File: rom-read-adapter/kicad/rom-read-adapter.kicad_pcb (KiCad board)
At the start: 2 copper layers, 100 x 100 mm, 27 parts

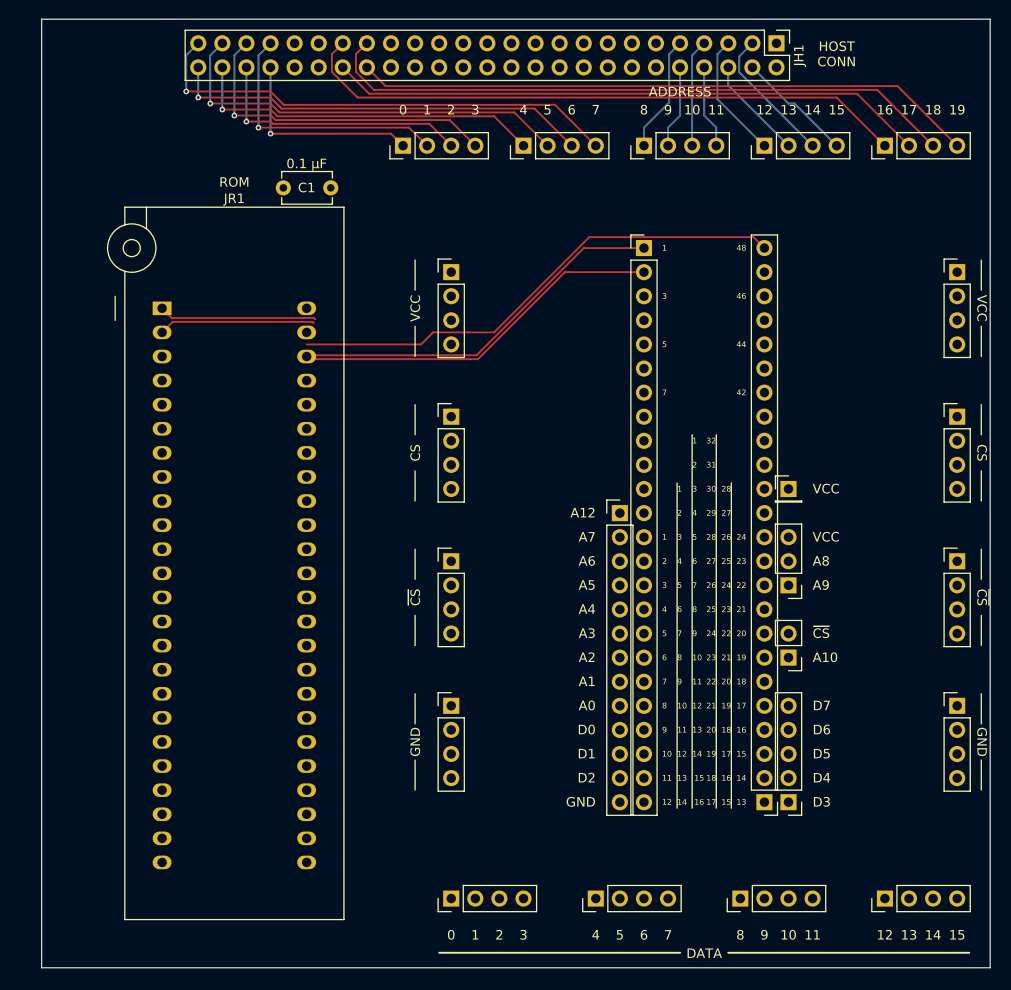
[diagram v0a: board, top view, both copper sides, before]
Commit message: WIP rom-read-adapter pcb: Add VCC/GND netclass; route D0-D8 non-default jumpers
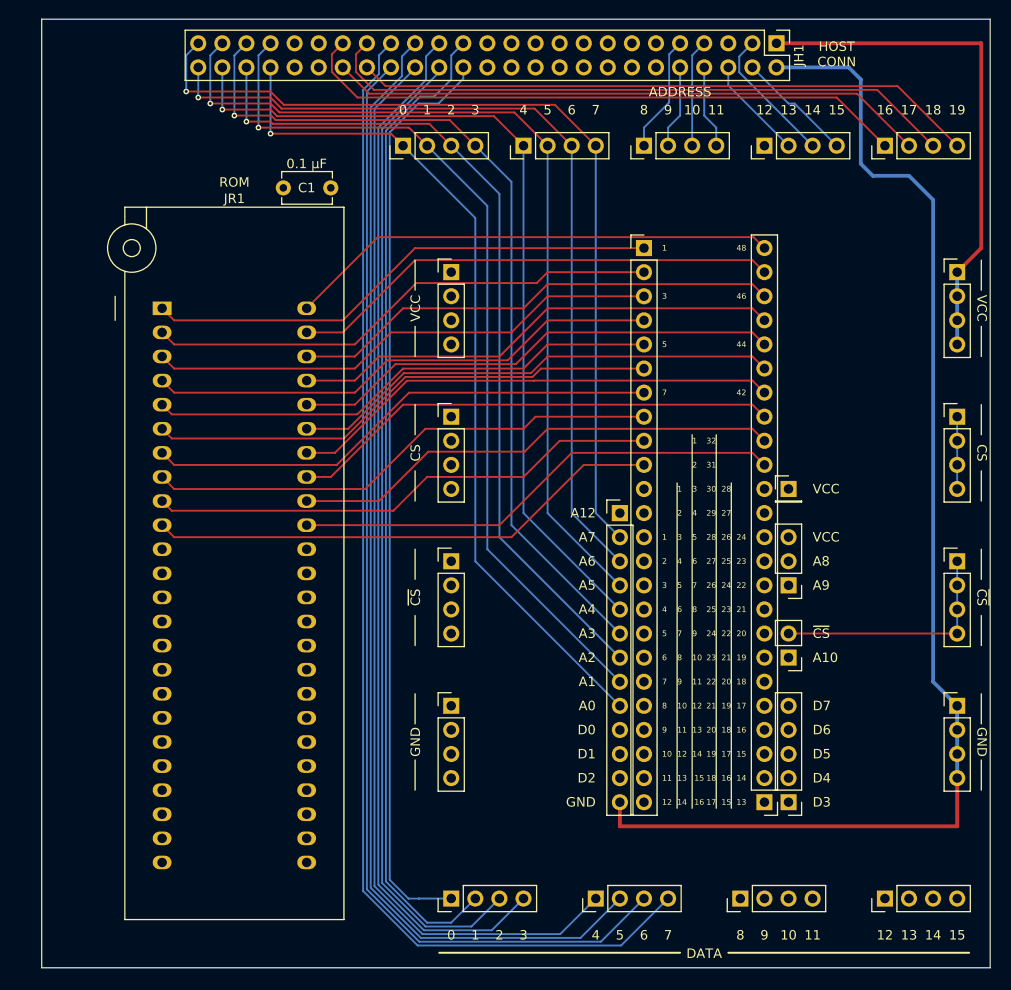
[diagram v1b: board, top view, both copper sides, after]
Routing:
- net GND: track 0.00 -> 132.7 mm
- net D7: track 0.00 -> 127.2 mm
- net D5: track 0.00 -> 121.1 mm
- net D6: track 0.00 -> 121.1 mm
- net D4: track 0.00 -> 115.1 mm
- net D3: track 0.00 -> 110.0 mm
- net D1: track 0.00 -> 104.9 mm
- net D2: track 0.00 -> 104.0 mm
- net D0: track 0.01 -> 97.4 mm
- net A0: track 21.5 -> 90.0 mm
- net A1: track 28.0 -> 92.9 mm
- net A2: track 28.4 -> 89.7 mm
- net A3: track 34.9 -> 92.6 mm
- net Net-(JR1-Pin_8): track 0.00 -> 54.5 mm
- net Net-(JR1-Pin_7): track 0.00 -> 54.5 mm
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
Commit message: WIP rom-read-adapter pcb: More routing; hit default pins problem
The default pins are in the way of getting ZIF socket pads connected
ZIF work area pin pads. We may try doing only right side pins on top
layer from this point on, and routing through the bottom layer for the
left side pins.
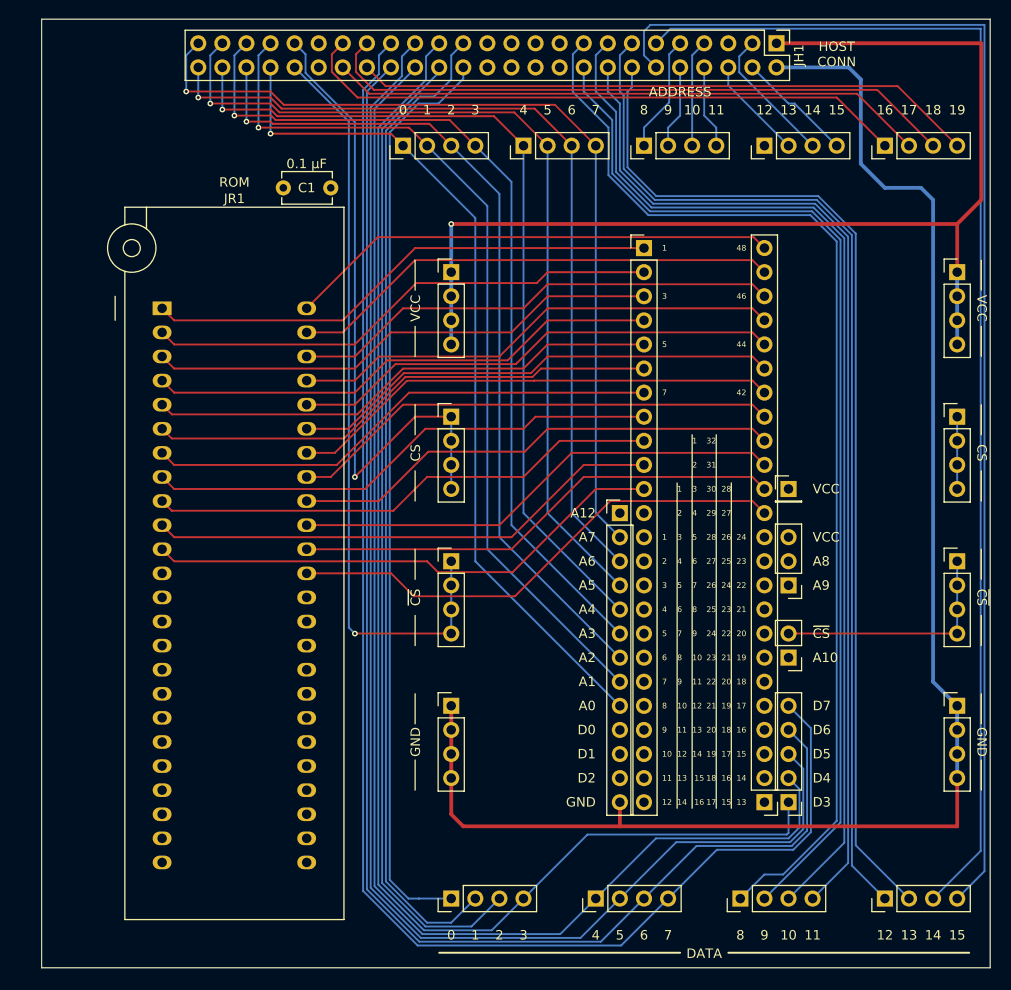
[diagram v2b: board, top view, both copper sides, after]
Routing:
- net D15: track 0.00 -> 133.8 mm
- net D14: track 0.00 -> 128.6 mm
- net D8: track 0.00 -> 117.5 mm
- net D10: track 0.00 -> 114.0 mm
- net D12: track 0.00 -> 112.3 mm
- net D9: track 0.00 -> 112.2 mm
- net D13: track 0.00 -> 110.1 mm
- net D11: track 0.00 -> 109.7 mm
- net ~{CS}: track 25.4 -> 105.5 mm, vias 0 -> 1
- net CS: track 7.62 -> 76.4 mm, vias 0 -> 1
- net VCC: track 54.4 -> 120.4 mm, vias 0 -> 1
- net Net-(JR1-Pin_11): track 0.00 -> 55.4 mm
- net Net-(JR1-Pin_37): track 0.00 -> 53.9 mm
- net Net-(JR1-Pin_38): track 0.00 -> 51.9 mm
- net D3: track 110.0 -> 144.1 mm
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
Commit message: WIP rom-read-adapter pcb: Routed ZIF 25-37 to work area, need to figure 12-24.
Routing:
- net Net-(JR1-Pin_35): track 0.00 -> 54.4 mm
- net Net-(JR1-Pin_36): track 0.00 -> 53.9 mm
- net Net-(JR1-Pin_34): track 0.00 -> 52.7 mm
- net Net-(JR1-Pin_28): track 0.00 -> 51.9 mm
- net Net-(JR1-Pin_26): track 0.00 -> 51.9 mm
- net Net-(JR1-Pin_32): track 0.00 -> 51.9 mm
- net Net-(JR1-Pin_31): track 0.00 -> 51.9 mm
- net Net-(JR1-Pin_30): track 0.00 -> 51.9 mm
- net Net-(JR1-Pin_27): track 0.00 -> 51.9 mm
- net Net-(JR1-Pin_33): track 0.00 -> 51.9 mm
- net Net-(JR1-Pin_29): track 0.00 -> 51.9 mm
- net Net-(JR1-Pin_25): track 0.00 -> 51.9 mm
- net D0: track 97.4 -> 122.6 mm
- net D1: track 104.9 -> 127.2 mm
- net D2: track 104.0 -> 123.4 mm
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
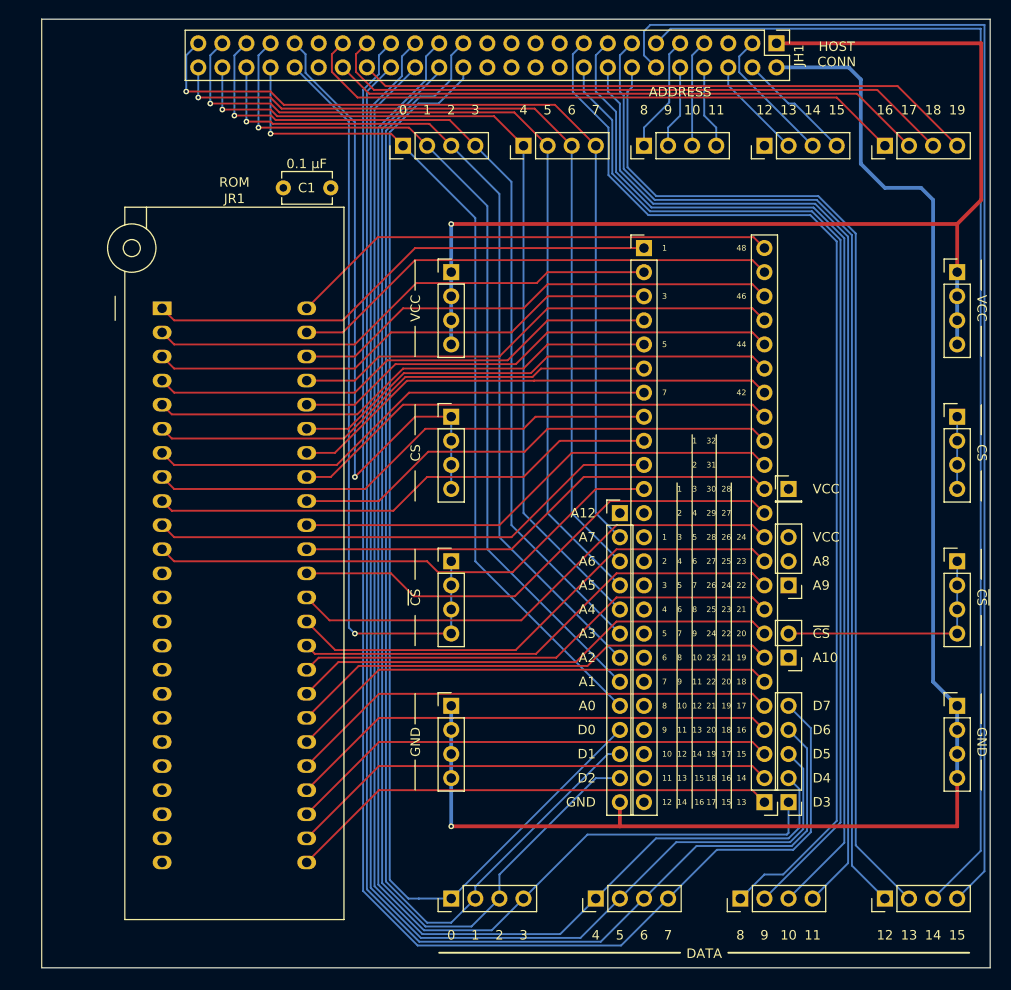
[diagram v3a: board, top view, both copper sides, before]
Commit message: WIP rom-read-adapter pcb: Everything routed except bypass cap
We need to figure out the best physical position for the bypass cap.
Ideally it should be as close as possible to the device pins
themselves, but we don't know which device pins are power; those are
determined half way across the board in the work area. So maybe place
it across the pin 12/24 GND and pin 24/24 VCC? Probably wants to be an
axial in that case, perhaps positioned top-to-bottom in the RHS
between the default jumpers and the VCC/CS/¬CS/GND jumpers.
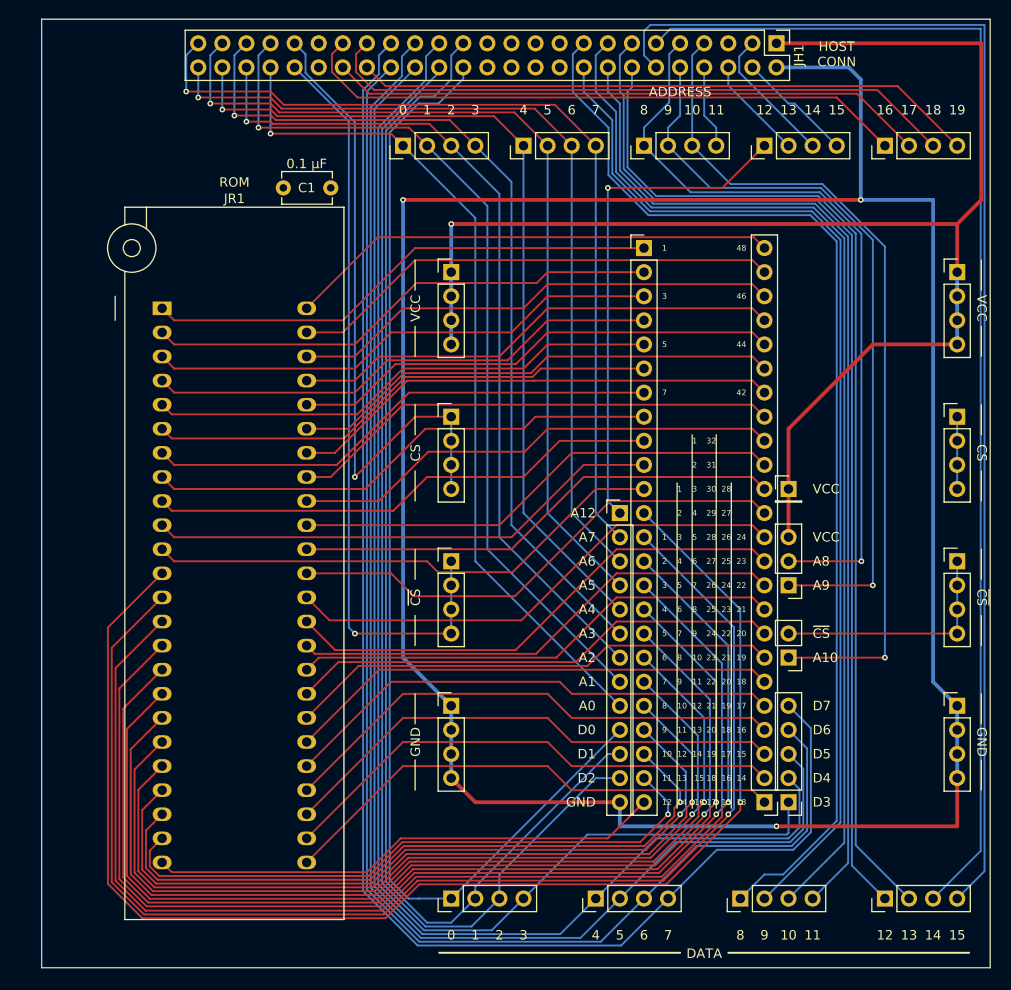
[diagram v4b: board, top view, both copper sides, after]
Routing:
- net Net-(JR1-Pin_12): track 0.00 -> 143.5 mm, vias 0 -> 1
- net Net-(JR1-Pin_13): track 0.00 -> 136.5 mm, vias 0 -> 1
- net Net-(JR1-Pin_14): track 0.00 -> 129.6 mm, vias 0 -> 1
- net Net-(JR1-Pin_15): track 0.00 -> 122.5 mm, vias 0 -> 1
- net Net-(JR1-Pin_16): track 0.00 -> 115.6 mm, vias 0 -> 1
- net Net-(JR1-Pin_17): track 0.00 -> 108.6 mm, vias 0 -> 1
- net GND: track 163.2 -> 265.1 mm, vias 1 -> 3
- net Net-(JR1-Pin_18): track 0.00 -> 101.7 mm, vias 0 -> 1
- net Net-(JR1-Pin_19): track 0.00 -> 94.6 mm, vias 0 -> 1
- net Net-(JR1-Pin_20): track 0.00 -> 87.7 mm, vias 0 -> 1
- net Net-(JR1-Pin_21): track 0.00 -> 80.7 mm, vias 0 -> 1
- net A10: track 11.3 -> 89.5 mm, vias 0 -> 1
- net Net-(JR1-Pin_22): track 0.00 -> 73.7 mm, vias 0 -> 1
- net A9: track 8.78 -> 79.8 mm, vias 0 -> 1
- net A8: track 12.4 -> 81.3 mm, vias 0 -> 1
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
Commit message: WIP rom-read-adapter: Replace disc cap with axial; all traces routed
We've gone with the solution mentioned in the previous commit message,
where we put an axial cap kinda-near the GND and VCC pins in the work
area. It could be closer, by moving some traces, or even by putting it
in between the socket pin connectors, though that would cover up lots
of pin numbers. (Maybe try it on the bottom? Still would moving some
traces to make room for the pads.)
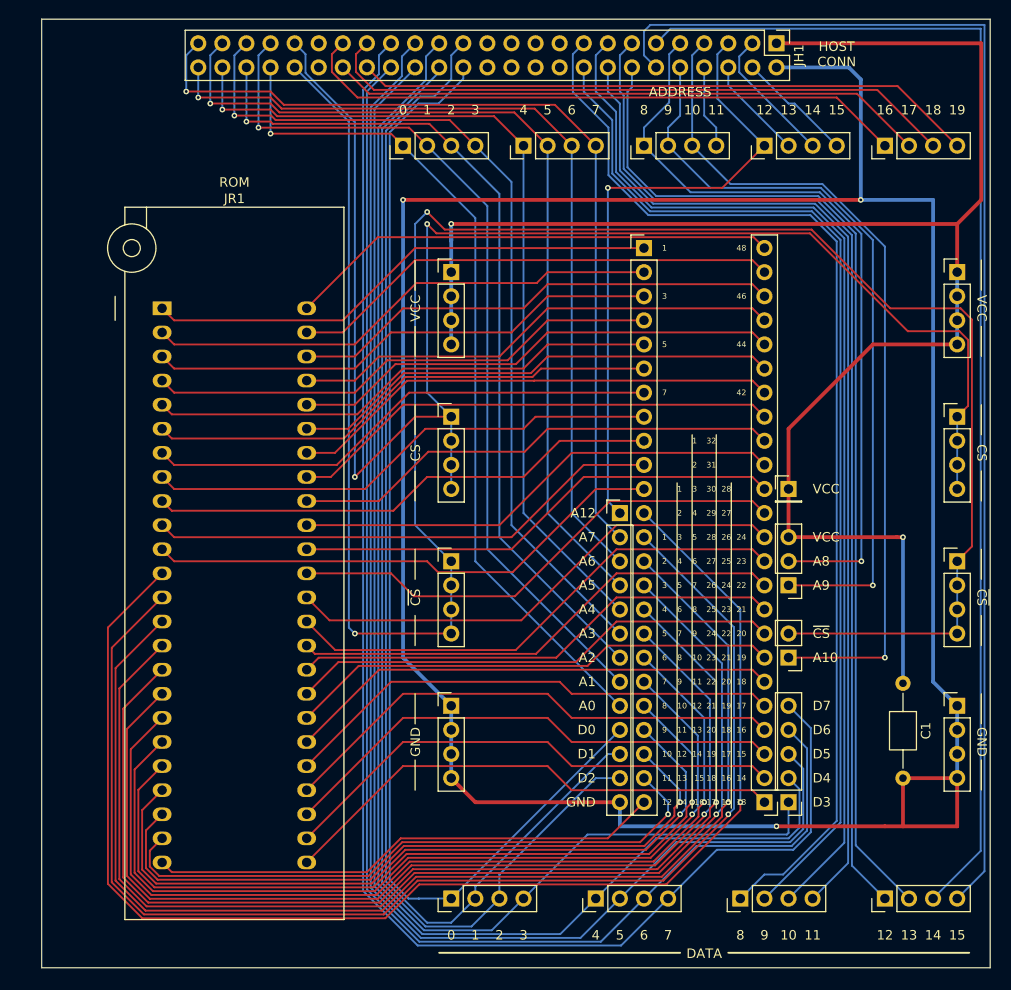
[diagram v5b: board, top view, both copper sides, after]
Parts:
- C1: footprint Capacitor_THT:C_Disc_D5.1mm_W3.2mm_P5.00mm -> Capacitor_THT:C_Axial_L3.8mm_D2.6mm_P10.00mm_Horizontal
- moved C1 83.6 mm to (192.4, 120.8), turned to -90 degrees
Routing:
- net ~{CS}: track 105.5 -> 232.7 mm, vias 1 -> 2
- net CS: track 76.4 -> 168.4 mm, vias 1 -> 2
- net VCC: track 153.3 -> 181.8 mm, vias 1 -> 2
- net A12: track 53.2 -> 66.5 mm
- net GND: track 265.1 -> 275.9 mm

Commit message: WIP rom-read-adapter pcb: Improved layout, but now needs re-routing
After checking a spin of the previous version, we have moved things
around to be more comfortable. Some additional useful text is also
added to the silkscreen.

This breaks all the traces, which we will fix up in a future commit.
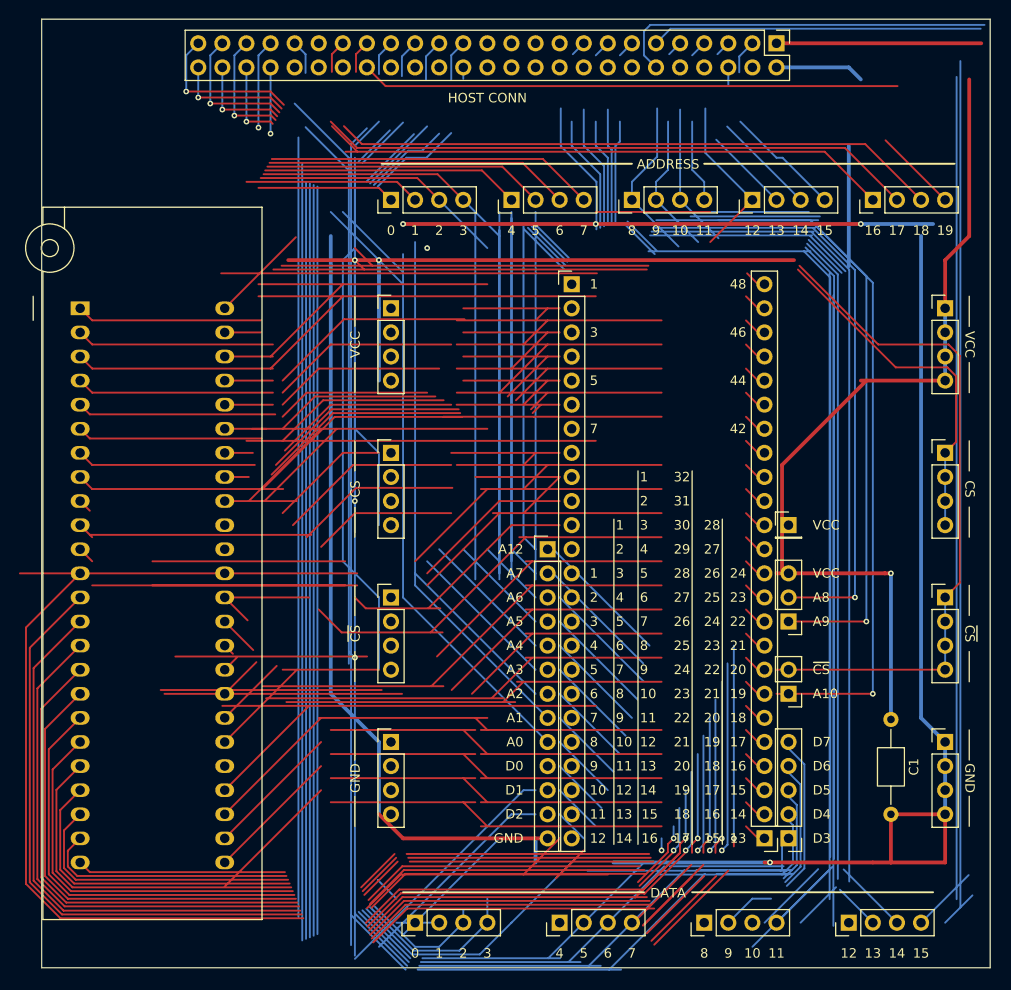
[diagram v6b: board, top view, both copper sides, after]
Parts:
- moved JR1 8.64 mm to (105.7, 81.3)
- moved JH2 8.52 mm to (154.9, 106.7)
- moved JR2 8.52 mm to (157.5, 78.7)
- moved JH33 7.41 mm to (138.4, 111.8)
- moved JH31 7.41 mm to (138.4, 81.3)
- moved JH32 7.41 mm to (138.4, 96.5)
- moved JH34 7.41 mm to (138.4, 127.0)
- moved JH12 5.85 mm to (151.1, 69.8)
- moved JH14 5.85 mm to (176.5, 69.8)
- moved JH15 5.85 mm to (189.2, 69.8)
- moved JH11 5.85 mm to (138.4, 69.8)
- moved JH13 5.85 mm to (163.8, 69.8)
- moved JH21 4.58 mm to (141.0, 146.1)
- moved JH22 4.58 mm to (156.2, 146.1)
- moved JH23 4.58 mm to (171.4, 146.1)
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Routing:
- net D11: track 109.7 -> 372.6 mm
- net D7: track 159.4 -> 390.2 mm
- net Net-(JR1-Pin_41): track 51.9 -> 234.7 mm
- net Net-(JR1-Pin_43): track 51.9 -> 201.7 mm
- net GND: track 275.9 -> 418.9 mm, vias 3 -> 2
- net D8: track 117.5 -> 1.63 mm
- net Net-(JR1-Pin_16): track 115.6 -> 211.1 mm, vias 1 -> 3
- net D15: track 133.8 -> 227.6 mm
- net D14: track 128.6 -> 34.9 mm
- net Net-(JR1-Pin_9): track 54.3 -> 144.7 mm
- net D12: track 112.3 -> 24.1 mm
- net D6: track 152.7 -> 68.6 mm
- net A12: track 66.5 -> 143.3 mm, vias 1 -> 3
- net D9: track 112.2 -> 53.9 mm
- net Net-(JR1-Pin_2): track 54.5 -> 102.1 mm
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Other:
- board text removed: "ROM"
